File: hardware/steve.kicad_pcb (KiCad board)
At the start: 4 copper layers, 50 x 100 mm, 10 parts, among them J1 Conn_ARM_JTAG_SWD_10, U1 STM32F407VGTx, Y1 12MHz, Y2 32.768kHz

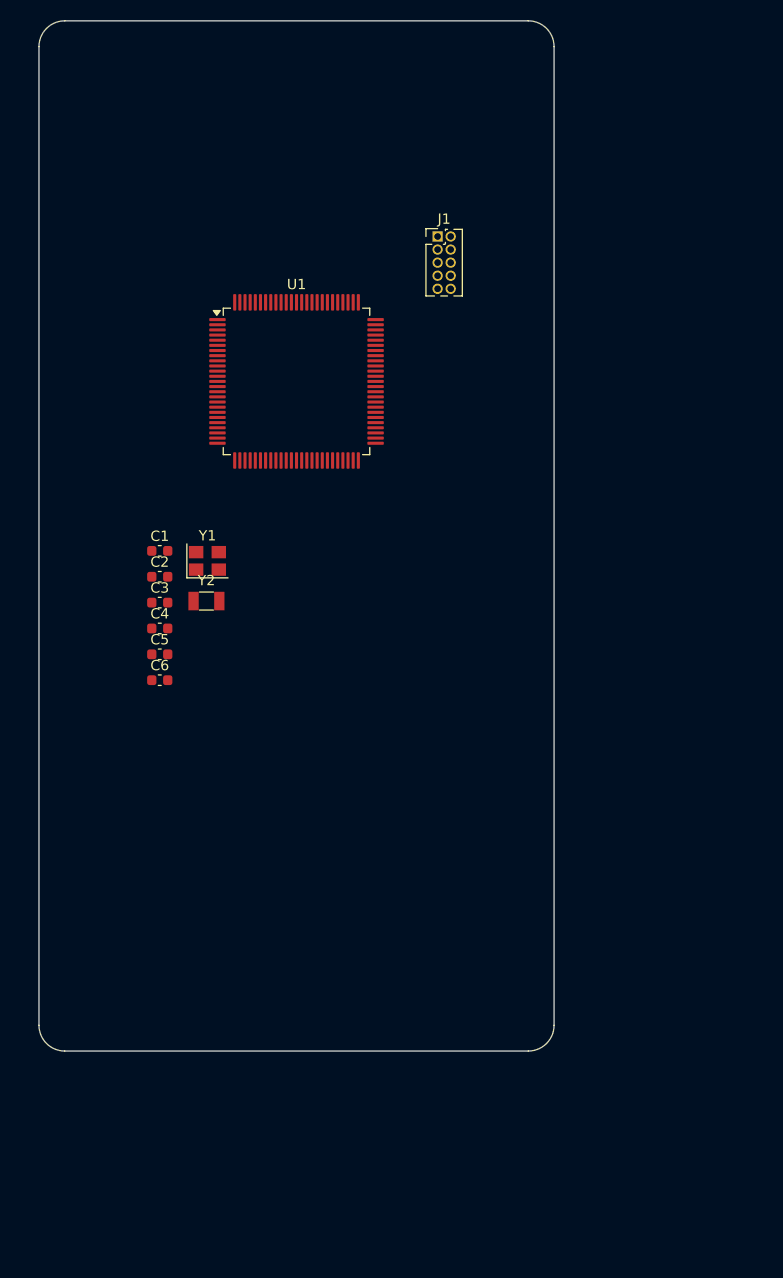
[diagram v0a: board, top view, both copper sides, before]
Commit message: Added 5V reg and other components
Added 5V regulator circuit to schematic. Added project libraries for imported symbols and footprints. Added additional components to schematic.
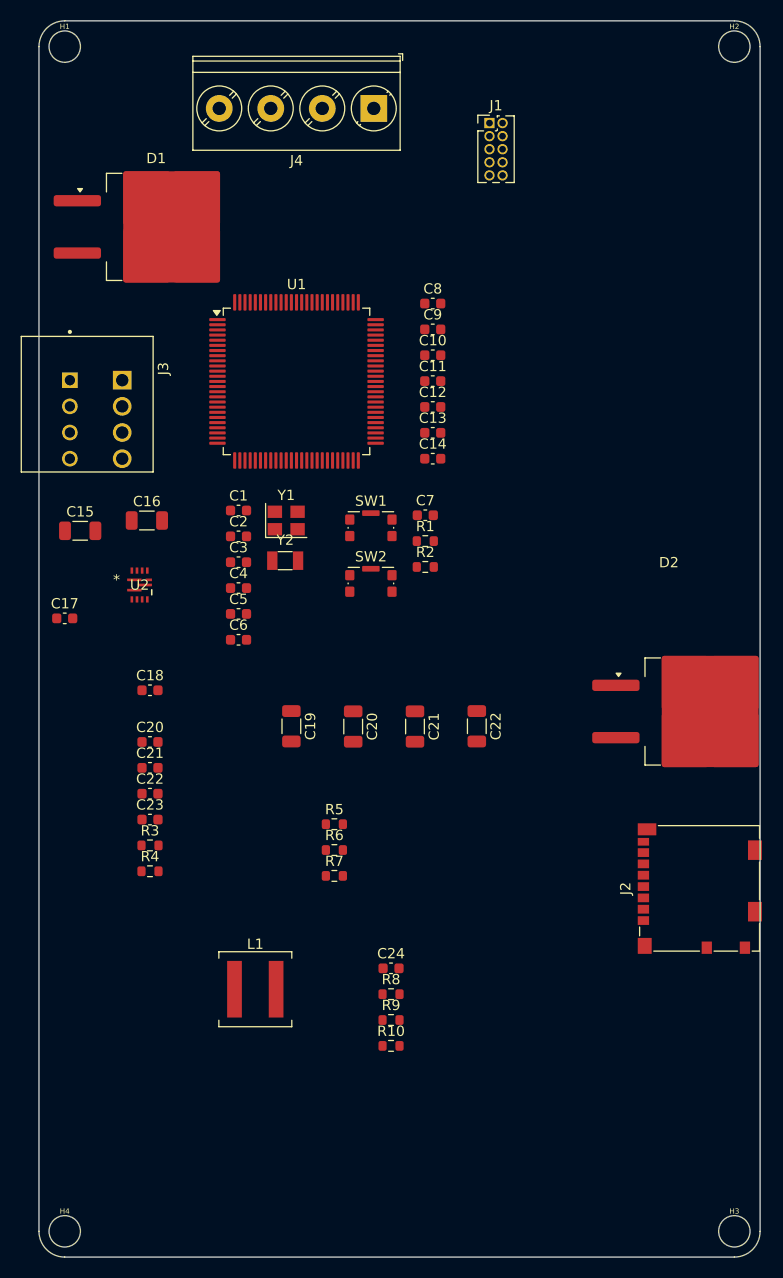
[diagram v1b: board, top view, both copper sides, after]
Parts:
- added C10: 0.1uF, Capacitor_SMD:C_0603_1608Metric, F.Cu at (88.2, 82.5)
- added C11: 0.1uF, Capacitor_SMD:C_0603_1608Metric, F.Cu at (88.2, 85.0)
- added C12: 4.7uF, Capacitor_SMD:C_0603_1608Metric, F.Cu at (88.2, 87.5)
- added C13: 1.0uF, Capacitor_SMD:C_0603_1608Metric, F.Cu at (88.2, 90.0)
- added C14: 1.0uF, Capacitor_SMD:C_0603_1608Metric, F.Cu at (88.2, 92.5)
- added C15: 10uF, Capacitor_SMD:C_1206_3216Metric, F.Cu at (54.0, 99.5)
- added C16: 10uF, Capacitor_SMD:C_1206_3216Metric, F.Cu at (60.5, 98.5)
- added C17: 0.1uF, Capacitor_SMD:C_0603_1608Metric, F.Cu at (52.5, 108.0)
- added C18: 1.0uF, Capacitor_SMD:C_0603_1608Metric, F.Cu at (60.8, 115.0)
- added C19: 22uF, Capacitor_SMD:C_1206_3216Metric, F.Cu at (74.5, 118.5)
- added C20: 22uF, Capacitor_SMD:C_0603_1608Metric, F.Cu at (60.8, 120.0)
- added C20: 22uF, Capacitor_SMD:C_1206_3216Metric, F.Cu at (80.5, 118.5)
- added C21: 22uF, Capacitor_SMD:C_0603_1608Metric, F.Cu at (60.8, 122.5)
- added C21: 22uF, Capacitor_SMD:C_1206_3216Metric, F.Cu at (86.5, 118.5)
- added C22: 22uF, Capacitor_SMD:C_1206_3216Metric, F.Cu at (92.5, 118.5)
- added C22: 22uF, Capacitor_SMD:C_0603_1608Metric, F.Cu at (60.8, 125.0)
- added C23: 0.1uF, Capacitor_SMD:C_0603_1608Metric, F.Cu at (60.8, 127.5)
- added C24: 22pF, Capacitor_SMD:C_0603_1608Metric, F.Cu at (84.2, 142.0)
- added C7: 0.1uF, Capacitor_SMD:C_0603_1608Metric, F.Cu at (87.5, 98.0)
- added C8: 0.1uF, Capacitor_SMD:C_0603_1608Metric, F.Cu at (88.2, 77.4)
- added C9: 0.1uF, Capacitor_SMD:C_0603_1608Metric, F.Cu at (88.2, 80.0)
- added D1: RECTIFIER, SCHOTTKY, 10A per diode, 200V, Package_TO_SOT_SMD:TO-263-2, F.Cu at (61.4, 70.0)
- added D2: RECTIFIER, SCHOTTKY, 10A per diode, 200V, Package_TO_SOT_SMD:TO-263-2, F.Cu at (113.7, 117.0)
- added H1: STAND-OFFTIGHT, SparkFun_STM32 Thing Plus:STAND-OFF-TIGHT, F.Cu at (52.5, 52.5)
- added H2: STAND-OFFTIGHT, SparkFun_STM32 Thing Plus:STAND-OFF-TIGHT, F.Cu at (117.5, 52.5)
- added H3: STAND-OFFTIGHT, SparkFun_STM32 Thing Plus:STAND-OFF-TIGHT, F.Cu at (117.5, 167.5)
- added H4: STAND-OFFTIGHT, SparkFun_STM32 Thing Plus:STAND-OFF-TIGHT, F.Cu at (52.5, 167.5)
- added J2: Micro_SD_Card_Det2, Connector_Card:microSD_HC_Molex_104031-0811, F.Cu at (114.1, 134.2)
- added J3: TE_1-2834015-4_Buchanan_WireMate_Screwless_Terminal_Block, Imported_Footprints:TE_1-2834015-4_Buchanan_WireMate_Screwless_Terminal_Block, F.Cu at (55.5, 88.7)
- added J4: Screw_Terminal_01x04, TerminalBlock_Phoenix:TerminalBlock_Phoenix_PT-1,5-4-5.0-H_1x04_P5.00mm_Horizontal, F.Cu at (82.5, 58.5)
- added L1: 2.2uH, Inductor_SMD:L_Coilcraft_XAL6060-XXX, F.Cu at (71.0, 144.0)
- added R1: 100k, Resistor_SMD:R_0603_1608Metric, F.Cu at (87.5, 100.5)
- added R10: 20k, Resistor_SMD:R_0603_1608Metric, F.Cu at (84.2, 149.5)
- added R2: 4.7k, Resistor_SMD:R_0603_1608Metric, F.Cu at (87.5, 103.0)
- added R3: 100k, Resistor_SMD:R_0603_1608Metric, F.Cu at (60.8, 130.0)
- added R4: 0k, Resistor_SMD:R_0603_1608Metric, F.Cu at (60.8, 132.6)
- added R5: 200k, Resistor_SMD:R_0603_1608Metric, F.Cu at (78.7, 128.0)
- added R6: 200k, Resistor_SMD:R_0603_1608Metric, F.Cu at (78.7, 130.5)
- added R7: 120k, Resistor_SMD:R_0603_1608Metric, F.Cu at (78.7, 133.0)
- added R8: 150k, Resistor_SMD:R_0603_1608Metric, F.Cu at (84.2, 144.5)
- added R9: 0k, Resistor_SMD:R_0603_1608Metric, F.Cu at (84.2, 147.0)
- added SW1: SW_SPST, Button_Switch_SMD:SW_SPST_CK_KMS2xxGP, F.Cu at (82.2, 99.2)
- added SW2: SW_SPST, Button_Switch_SMD:SW_SPST_CK_KMS2xxGP, F.Cu at (82.2, 104.6)
- added U2: TI_TPS51386RJNR_Regulator_Buck_8A, Imported_Footprints:TI_TPS51386RJNR_VQFN-HR_REG_BUCK_8A, F.Cu at (59.8, 104.8)
- moved J1 12.1 mm to (93.7, 59.9)
- moved C1 8.59 mm to (69.4, 97.5)
- moved C3 8.59 mm to (69.4, 102.5)
- moved C4 8.59 mm to (69.4, 105.1)
- moved C5 8.59 mm to (69.4, 107.6)
- moved C6 8.59 mm to (69.4, 110.1)
- moved Y2 8.59 mm to (73.9, 102.4)
- moved C2 8.59 mm to (69.4, 100.0)
- moved Y1 8.59 mm to (74.0, 98.5)
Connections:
- U1 pad 94: unconnected-(U1-BOOT0-Pad94) -> BOOT0
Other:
- board size 50 x 100 mm -> 70 x 120 mm

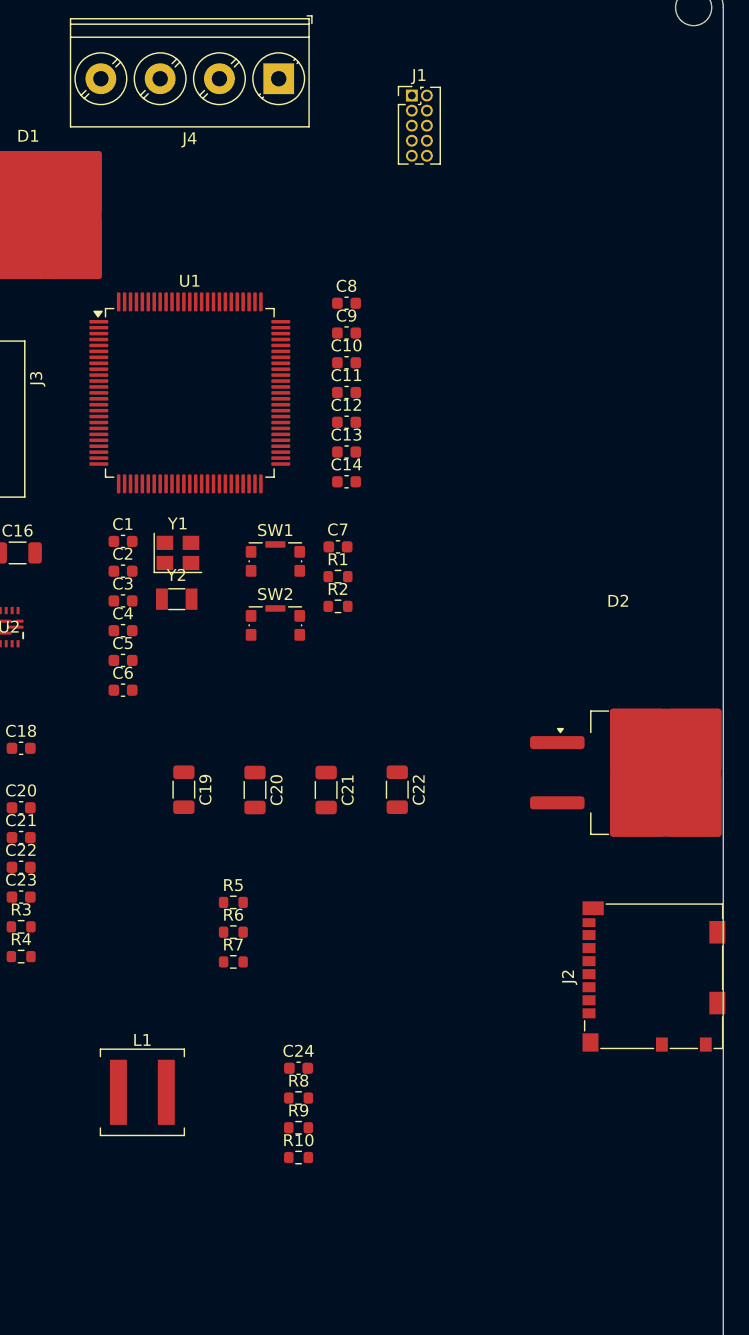
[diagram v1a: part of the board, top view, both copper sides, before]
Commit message: import BMP388, add BMP388 to pcb and sch
Import BMP388 symbol and footprint to project imports dir. Add BMP388 symbol to schematic and footprint to pcb.
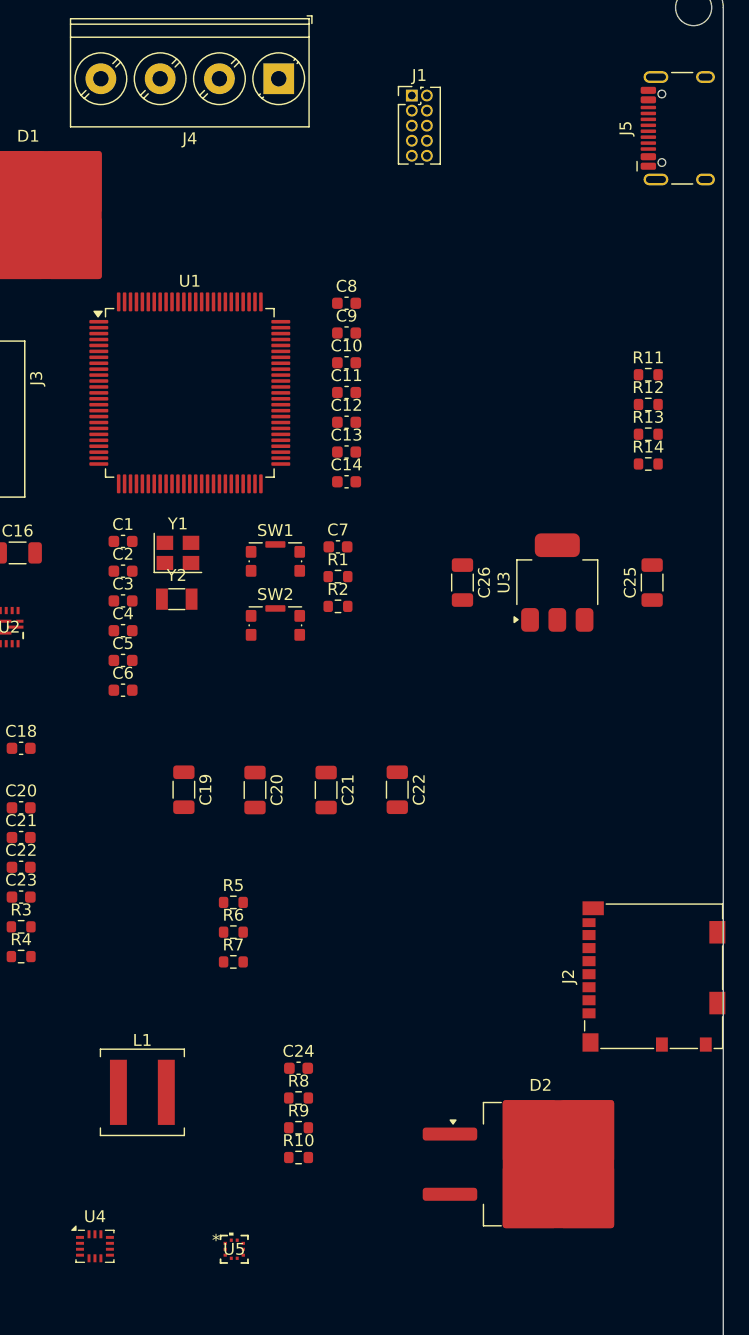
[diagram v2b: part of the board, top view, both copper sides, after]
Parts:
- added C25: 1.0uF, Capacitor_SMD:C_1206_3216Metric, F.Cu at (114.0, 101.0)
- added C26: 1.0uF, Capacitor_SMD:C_1206_3216Metric, F.Cu at (98.0, 101.0)
- added J5: USB_C_Receptacle_16P, Connector_USB:USB_C_Receptacle_HCTL_HC-TYPE-C-16P-01A, F.Cu at (117.4, 62.7)
- added R11: 22, Resistor_SMD:R_0603_1608Metric, F.Cu at (113.7, 83.5)
- added R12: 22, Resistor_SMD:R_0603_1608Metric, F.Cu at (113.7, 86.0)
- added R13: 5.1k, Resistor_SMD:R_0603_1608Metric, F.Cu at (113.7, 88.5)
- added R14: 5.1k, Resistor_SMD:R_0603_1608Metric, F.Cu at (113.7, 91.0)
- added U3: TLV1117LV33DCYR, Package_TO_SOT_SMD:SOT-223-3_TabPin2, F.Cu at (106.0, 101.0)
- added U4: BMI270, Package_LGA:Bosch_LGA-14_3x2.5mm_P0.5mm, F.Cu at (67.0, 157.0)
- added U5: BMP388, Imported_Footprints:QFN_BMP388_BOS, F.Cu at (78.8, 157.2)
- D2: value RECTIFIER, SCHOTTKY, 10A per diode, 200V -> SCHOTTKY ARR, 10A per, 200V
- moved D2 34.2 mm to (104.6, 150.1)
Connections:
- C19 pad 1: +5V -> +5V_BATT
- C20 pad 1: +5V -> +5V_BATT
- C21 pad 1: +5V -> +5V_BATT
- C22 pad 1: +5V -> +5V_BATT
- C24 pad 2: +5V -> +5V_BATT
- D2 pad 1: unconnected-(D2-A-Pad1) -> +5V_BATT
- D2 pad 2: unconnected-(D2-K-Pad2) -> +5V
- D2 pad 3: unconnected-(D2-A-Pad3) -> +5V_USB
- J3 pad 1_1: TEST_1 -> unconnected-(J3-1-Pad1_1)
- J3 pad 1_2: TEST_1 -> unconnected-(J3-1__1-Pad1_2)
- J3 pad 2_1: TEST_2 -> unconnected-(J3-2-Pad2_1)
- J3 pad 2_2: TEST_2 -> unconnected-(J3-2__1-Pad2_2)
- J3 pad 3_1: TEST_3 -> unconnected-(J3-3-Pad3_1)
- J3 pad 3_2: TEST_3 -> unconnected-(J3-3__1-Pad3_2)
- J3 pad 4_1: TEST_4 -> unconnected-(J3-4-Pad4_1)
- J3 pad 4_2: TEST_4 -> unconnected-(J3-4__1-Pad4_2)
- L1 pad 2: +5V -> +5V_BATT
- R8 pad 2: +5V -> +5V_BATT
- U1 pad 70: unconnected-(U1-PA11-Pad70) -> D-
- U1 pad 71: unconnected-(U1-PA12-Pad71) -> D+
